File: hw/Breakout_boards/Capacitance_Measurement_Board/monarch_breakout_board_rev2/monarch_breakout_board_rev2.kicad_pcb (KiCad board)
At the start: 2 copper layers, 23 x 27.1 mm, 24 parts, among them J1 5037630491, J2 5037630491, J3 5037630491, U1 FDC2214RGHR

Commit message: Breakout Boards Measurements
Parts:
- removed U1: FDC2214RGHR, FDC2214:RGH0016A
- added J4: 2200980471, Connector_Molex_Micro-Lock-Plus:Molex_Micro-Lock_2200980471_1x04_P1.25mm_Horizontal, F.Cu at (150.0, 52.2)
- added TP5: TestPoint, TestPoint:TestPoint_Keystone_5000-5004_Miniature, F.Cu at (144.1, 51.6)
- added TP6: TestPoint, TestPoint:TestPoint_Keystone_5000-5004_Miniature, F.Cu at (144.1, 56.0)
- added TP7: TestPoint, TestPoint:TestPoint_Keystone_5000-5004_Miniature, F.Cu at (144.1, 60.3)
- added TP8: TestPoint, TestPoint:TestPoint_Keystone_5000-5004_Miniature, F.Cu at (144.1, 64.7)
- added U2: FDC2214RGHR, FDC2214:RGH0016A, F.Cu at (161.0, 52.2)
- J1, J2, J3: value 5037630491 -> 2200980471; footprint Connector 4 Pin:CONN_5037630000-SD_04_MOL -> Connector_Molex_Micro-Lock-Plus:Molex_Micro-Lock_2200980471_1x04_P1.25mm_Horizontal
- moved TP3 13.2 mm to (97.0, 57.0)
- moved J3 10.9 mm to (108.1, 48.3), turned to -90 degrees
- moved TP1 5.66 mm to (112.9, 44.0)
- moved J2 2.48 mm to (129.0, 50.9)
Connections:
- C1 pad 1: Cap0+ -> /Cap0+
- C1 pad 2: Cap0- -> /Cap0-
- C2 pad 1: Cap1+ -> /Cap1+
- C2 pad 2: Cap1- -> /Cap1-
- C3 pad 1: Cap2+ -> /Cap2+
- C3 pad 2: Cap2- -> /Cap2-
- C4 pad 1: Cap3+ -> /Cap3+
- C4 pad 2: Cap3- -> /Cap3-
- J1 pad 1: +3V3 -> /Cap0+
- J1 pad 2: GND -> /Cap0-
- J1 pad 3: I2C4_SCL -> /Cap1+
- J1 pad 4: I2C4_SDA -> /Cap1-
- J2 pad 1: Cap0+ -> /Cap2+
- J2 pad 2: Cap0- -> /Cap2-
- J2 pad 3: Cap1+ -> /Cap3+
- J2 pad 4: Cap1- -> /Cap3-
- J3 pad 1: Cap2+ -> +3V3
- J3 pad 2: Cap2- -> GND
- J3 pad 3: Cap3+ -> /I2C4_SCL
- J3 pad 4: Cap3- -> /I2C4_SDA
- L1 pad 1: Cap0+ -> /Cap0+
- L1 pad 2: Cap0- -> /Cap0-
- L2 pad 1: Cap1+ -> /Cap1+
- L2 pad 2: Cap1- -> /Cap1-
- L3 pad 1: Cap2+ -> /Cap2+
- L3 pad 2: Cap2- -> /Cap2-
- L4 pad 1: Cap3+ -> /Cap3+
- L4 pad 2: Cap3- -> /Cap3-
- TP1 pad 1: I2C4_SCL -> /I2C4_SCL
- TP3 pad 1: I2C4_SDA -> +3V3
- TP4 pad 1: +3V3 -> /I2C4_SDA
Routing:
- net I2C4_SCL: track 18.6 -> 0.00 mm, vias 2 -> 0
- net I2C4_SDA: track 18.1 -> 0.00 mm, vias 2 -> 0
- net /I2C4_SCL: track 0.00 -> 13.6 mm, vias 0 -> 2
- net +3V3: track 27.1 -> 40.6 mm, vias 0 -> 2
- net Cap0+: track 8.78 -> 0.00 mm
- net /Cap0+: track 0.00 -> 8.78 mm
- net Cap1-: track 8.29 -> 0.00 mm
- net /Cap1-: track 0.00 -> 8.29 mm
- net Cap3-: track 8.12 -> 0.00 mm
- net /Cap3-: track 0.00 -> 8.12 mm
- net Cap2+: track 7.90 -> 0.00 mm
- net /Cap2+: track 0.00 -> 7.90 mm
- net Cap0-: track 7.71 -> 0.00 mm
- net /Cap0-: track 0.00 -> 7.71 mm
- net Cap1+: track 7.39 -> 0.00 mm
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
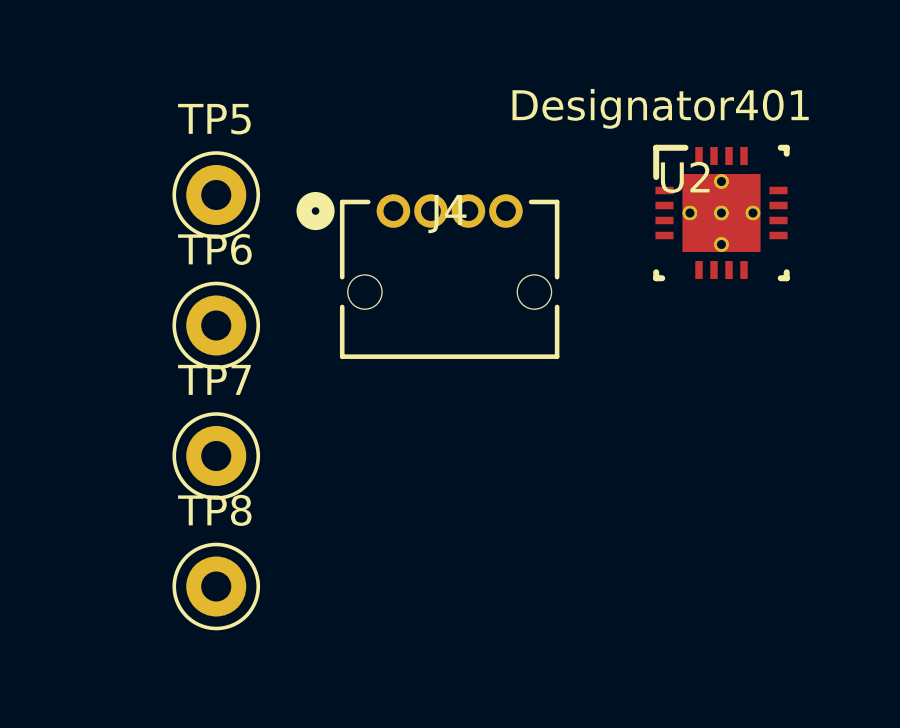
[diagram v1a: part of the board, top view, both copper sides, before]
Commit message: Accelerometer Board Removed
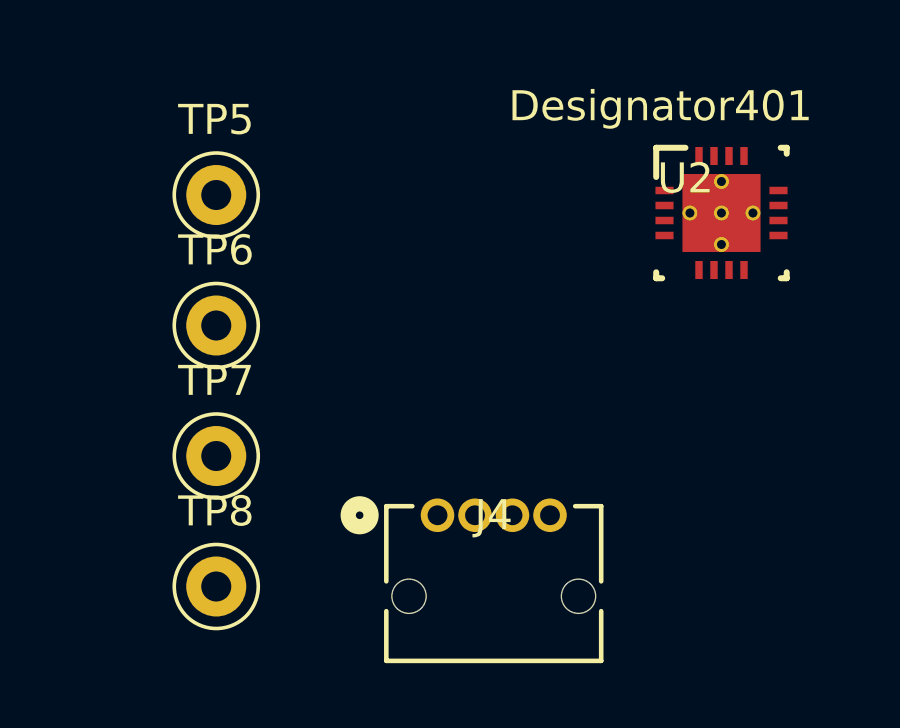
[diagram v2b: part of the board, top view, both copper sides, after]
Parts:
- moved J4 10.2 mm to (151.5, 62.3)
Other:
- board text added: "Rev2 - 08//2026"
- board text removed: "Rev1 - 3/12/2026"

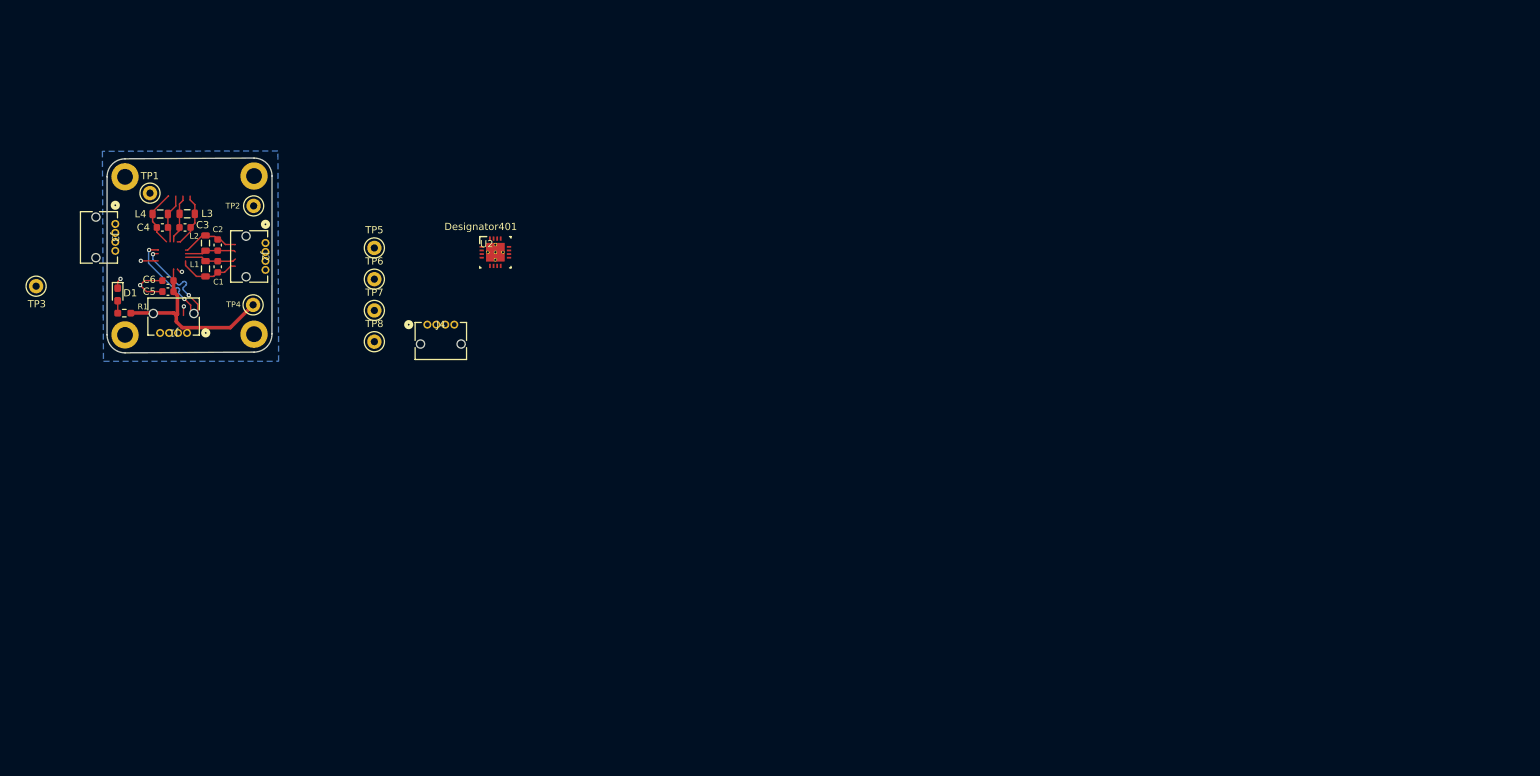
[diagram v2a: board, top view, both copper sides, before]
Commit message: Capacitance Board Schematic Done - Ran into issue with too big of BNC connectors
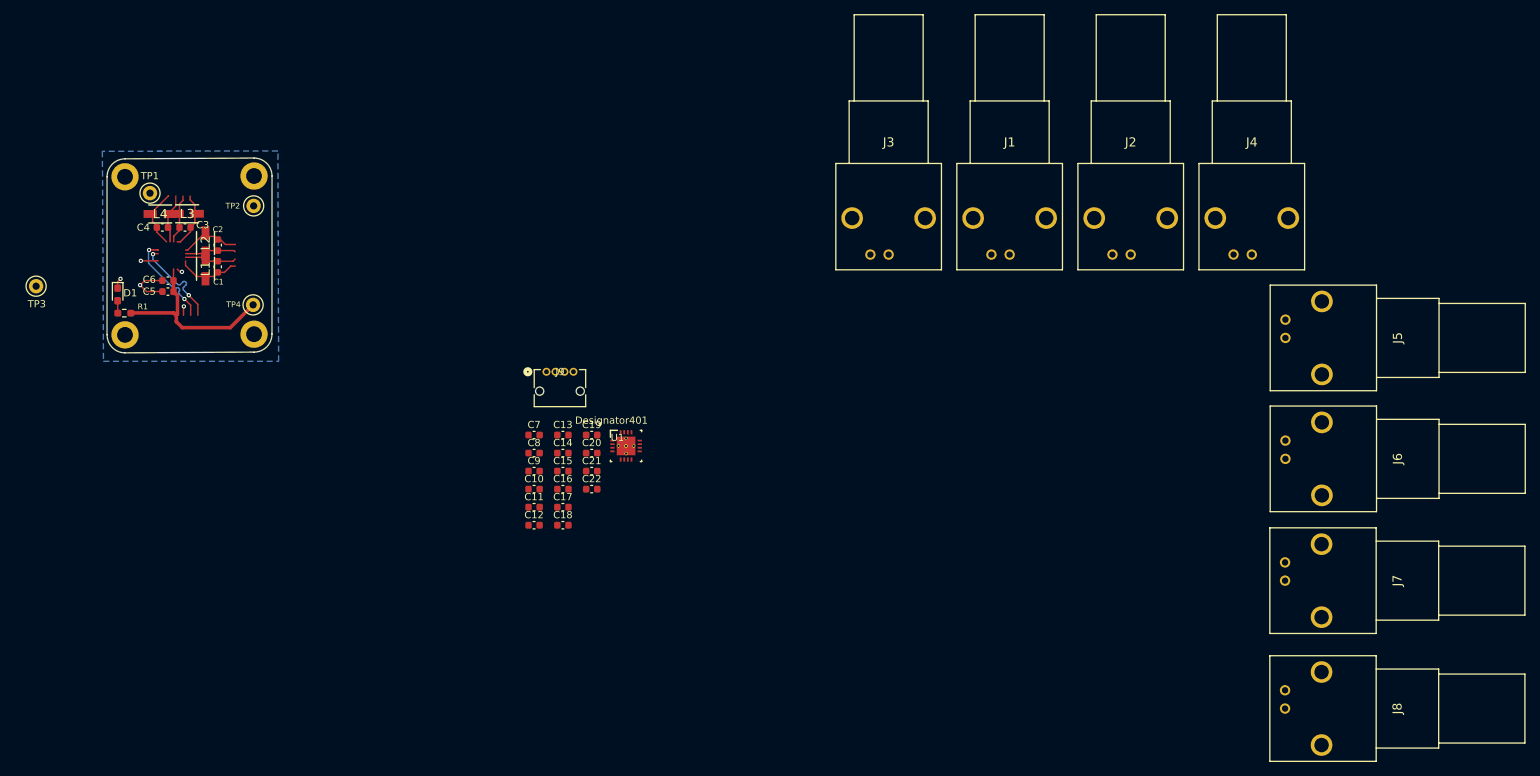
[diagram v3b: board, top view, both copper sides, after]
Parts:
- removed TP5, TP6, TP7, TP8: TestPoint, TestPoint:TestPoint_Keystone_5000-5004_Miniature
- removed U2: FDC2214RGHR, FDC2214:RGH0016A
- added C10: 18pF, Capacitor_SMD:C_0603_1608Metric, F.Cu at (166.4, 85.2)
- added C11: 18pF, Capacitor_SMD:C_0603_1608Metric, F.Cu at (166.4, 87.7)
- added C12: 18pF, Capacitor_SMD:C_0603_1608Metric, F.Cu at (166.4, 90.2)
- added C13: 18pF, Capacitor_SMD:C_0603_1608Metric, F.Cu at (170.4, 77.7)
- added C14: 18pF, Capacitor_SMD:C_0603_1608Metric, F.Cu at (170.4, 80.2)
- added C15: 18pF, Capacitor_SMD:C_0603_1608Metric, F.Cu at (170.4, 82.7)
- added C16: 18pF, Capacitor_SMD:C_0603_1608Metric, F.Cu at (170.4, 85.2)
- added C17: 18pF, Capacitor_SMD:C_0603_1608Metric, F.Cu at (170.4, 87.7)
- added C18: 18pF, Capacitor_SMD:C_0603_1608Metric, F.Cu at (170.4, 90.2)
- added C19: 18pF, Capacitor_SMD:C_0603_1608Metric, F.Cu at (174.4, 77.7)
- added C20: 18pF, Capacitor_SMD:C_0603_1608Metric, F.Cu at (174.4, 80.2)
- added C21: 1uF, Capacitor_SMD:C_0603_1608Metric, F.Cu at (174.4, 82.7)
- added C22: 0.1 uF, Capacitor_SMD:C_0603_1608Metric, F.Cu at (174.4, 85.2)
- added C7: 18pF, Capacitor_SMD:C_0603_1608Metric, F.Cu at (166.4, 77.7)
- added C8: 18pF, Capacitor_SMD:C_0603_1608Metric, F.Cu at (166.4, 80.2)
- added C9: 18pF, Capacitor_SMD:C_0603_1608Metric, F.Cu at (166.4, 82.7)
- added J5: Conn_Coaxial, BNC_Adam_Tech:RF101AD0075M, F.Cu at (270.9, 64.2)
- added J6: Conn_Coaxial, BNC_Adam_Tech:RF101AD0075M, F.Cu at (270.9, 81.0)
- added J7: Conn_Coaxial, BNC_Adam_Tech:RF101AD0075M, F.Cu at (270.9, 97.9)
- added J8: Conn_Coaxial, BNC_Adam_Tech:RF101AD0075M, F.Cu at (270.9, 115.7)
- added J9: 2200980471, Connector_Molex_Micro-Lock-Plus:Molex_Micro-Lock_2200980471_1x04_P1.25mm_Horizontal, F.Cu at (168.1, 68.9)
- added U1: FDC2214RGHR, FDC2214:RGH0016A, F.Cu at (179.2, 79.2)
- C5: value 1uF -> 18pF
- C6: value 0.1 uF -> 18pF
- J1, J2, J3, J4: value 2200980471 -> Conn_Coaxial; footprint Connector_Molex_Micro-Lock-Plus:Molex_Micro-Lock_2200980471_1x04_P1.25mm_Horizontal -> BNC_Adam_Tech:RF101AD0075M
- L1, L2, L3, L4: footprint Inductor_SMD:L_0805_2012Metric -> Inductor_Bourns:INDM3225X240N
- moved J2 120.4 mm to (249.4, 52.5), turned to 0 degrees
- moved J4 115.2 mm to (266.2, 52.5)
- moved J1 115.0 mm to (232.5, 52.5), turned to 0 degrees
- moved J3 107.7 mm to (215.7, 52.5), turned to 0 degrees
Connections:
- C5 pad 1: GND -> /Cap1+
- C5 pad 2: +3V3 -> GND
- C6 pad 2: +3V3 -> /Cap1-
- J1 pad 2: /Cap0- -> GND
- J2 pad 1: /Cap2+ -> /Cap0-
- J2 pad 2: /Cap2- -> GND
- J3 pad 1: +3V3 -> /Cap1+
- J4 pad 1: /I2C4_SCL -> /Cap1-
- J4 pad 2: /I2C4_SDA -> GND
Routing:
- net +3V3: track 40.6 -> 56.7 mm, vias 2 -> 4
- net /I2C4_SCL: track 13.6 -> 0.00 mm, vias 2 -> 0
- net GND: track 12.8 -> 10.4 mm

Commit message: Board Expansion + Front Layer Work
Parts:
- removed J5, J6, J7, J8: Conn_Coaxial, BNC_Adam_Tech:RF101AD0075M
- J1, J2, J3, J4: value Conn_Coaxial -> Conn_01x02; footprint BNC_Adam_Tech:RF101AD0075M -> Connector_Molex_Micro-Lock-Plus:Molex_Micro-Lock_2200980271_1x02_P1.25mm_Horizontal
- moved J4 150.9 mm to (115.7, 42.1), turned to 180 degrees
- moved J2 120.9 mm to (128.4, 52.2), turned to 90 degrees
- moved J1 104.2 mm to (128.4, 57.4), turned to 90 degrees
- moved J3 95.4 mm to (120.9, 42.1), turned to 180 degrees
- moved U1 67.4 mm to (116.7, 53.9)
- moved C5 52.1 mm to (167.4, 58.5)
- moved C6 52.1 mm to (167.4, 57.0)
- moved J9 51.1 mm to (117.5, 61.1)
- moved TP4 19.0 mm to (144.6, 67.2)
- moved TP1 18.3 mm to (95.7, 50.3)
- moved C3 4.30 mm to (120.9, 45.8)
- moved C1 3.99 mm to (124.8, 57.4)
- moved L1 3.55 mm to (122.3, 57.6)
- moved L3 3.17 mm to (121.0, 48.2)
- moved C4 3.15 mm to (115.7, 45.8)
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- renumbered TP2 to GND
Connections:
- J1 pad 2: GND -> /Cap0-
- J2 pad 1: /Cap0- -> /Cap1+
- J2 pad 2: GND -> /Cap1-
- J3 pad 1: /Cap1+ -> /Cap2+
- J3 pad 2: GND -> /Cap2-
- J4 pad 1: /Cap1- -> /Cap3+
- J4 pad 2: GND -> /Cap3-
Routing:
- net +3V3: track 56.7 -> 0.04 mm, vias 4 -> 0
- net GND: track 10.4 -> 1.47 mm, vias 5 -> 1
- net /Cap0+: track 8.78 -> 0.00 mm
- net /Cap1-: track 8.29 -> 0.00 mm
- net /Cap3-: track 8.12 -> 0.00 mm
- net /Cap2+: track 7.90 -> 0.00 mm
- net /Cap0-: track 7.71 -> 0.00 mm
- net /Cap1+: track 7.39 -> 0.00 mm
- net /Cap3+: track 6.95 -> 0.00 mm
- net /Cap2-: track 6.91 -> 0.00 mm
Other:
- board size 23 x 27.1 mm -> 24.6 x 27.1 mm

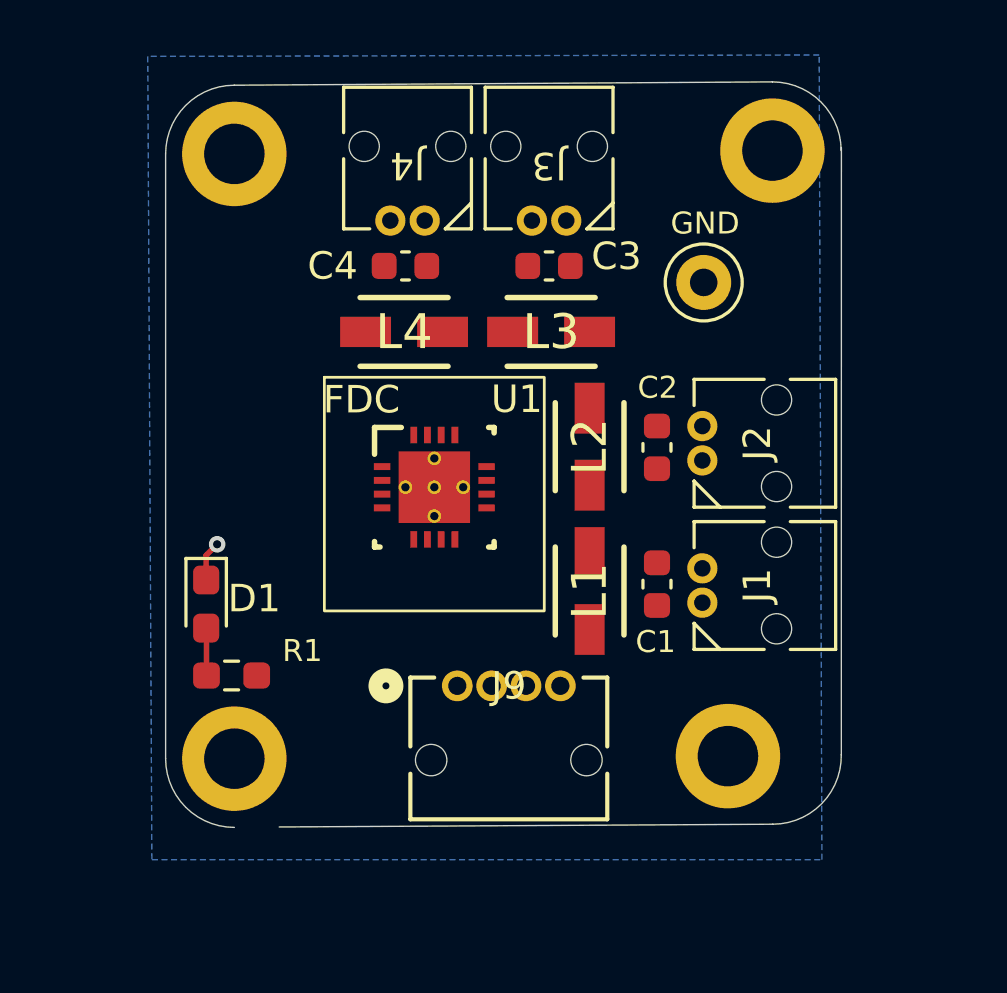
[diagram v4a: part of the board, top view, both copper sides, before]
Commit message: First layer + via additions
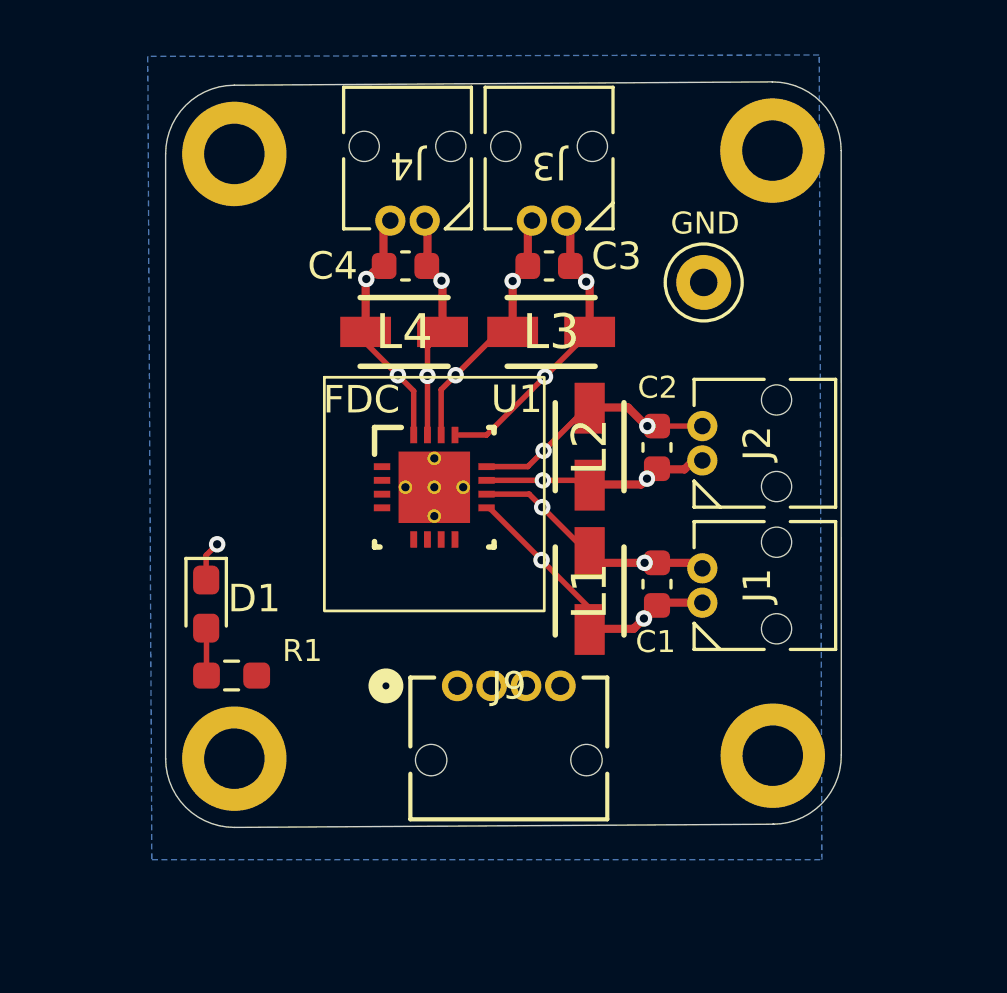
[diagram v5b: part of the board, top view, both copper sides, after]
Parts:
- moved H4 1.63 mm to (129.0, 63.6)
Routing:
- net /Cap2+: track 0.00 -> 10.9 mm, vias 0 -> 2
- net /Cap0+: track 0.00 -> 10.5 mm, vias 0 -> 2
- net /Cap2-: track 0.00 -> 9.46 mm, vias 0 -> 2
- net /Cap3-: track 0.00 -> 9.02 mm, vias 0 -> 2
- net /Cap1-: track 0.00 -> 9.02 mm, vias 0 -> 2
- net /Cap0-: track 0.00 -> 8.97 mm, vias 0 -> 2
- net /Cap3+: track 0.00 -> 8.32 mm, vias 0 -> 2
- net /Cap1+: track 0.00 -> 8.32 mm, vias 0 -> 2
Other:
- outline, holes or cut-outs redrawn
